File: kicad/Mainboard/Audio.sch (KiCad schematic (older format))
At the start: 66 parts, among them J10 MIC_EXT, J12 SPK_EXT, Q4 BSS138, Q5 BSS138, SW1 INT_PTT_SW, U10 LM386, U8 HEF4066B, U9 OPA340UA

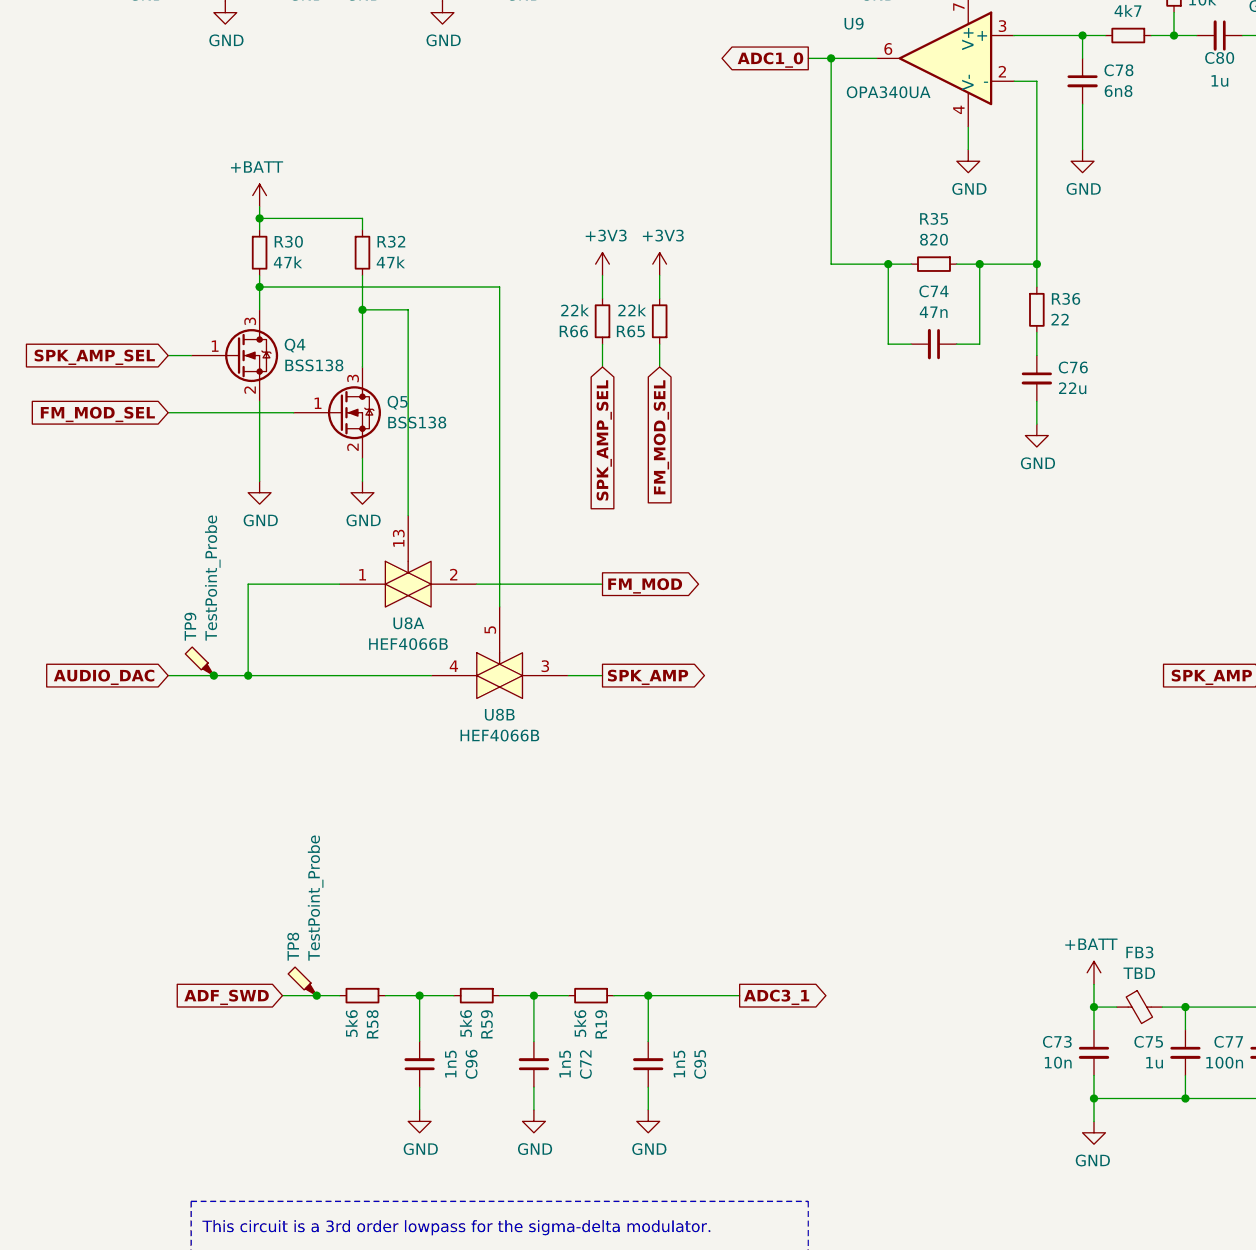
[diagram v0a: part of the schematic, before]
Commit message: added a JCx symbols - these are Jumper Cables - them are used to avoid EMI diseaster when trying to route Power signals under RF 50 ohm trace - also added them to PCB +  Schematic in PDF plotted; TODO - more signal integrity improvement
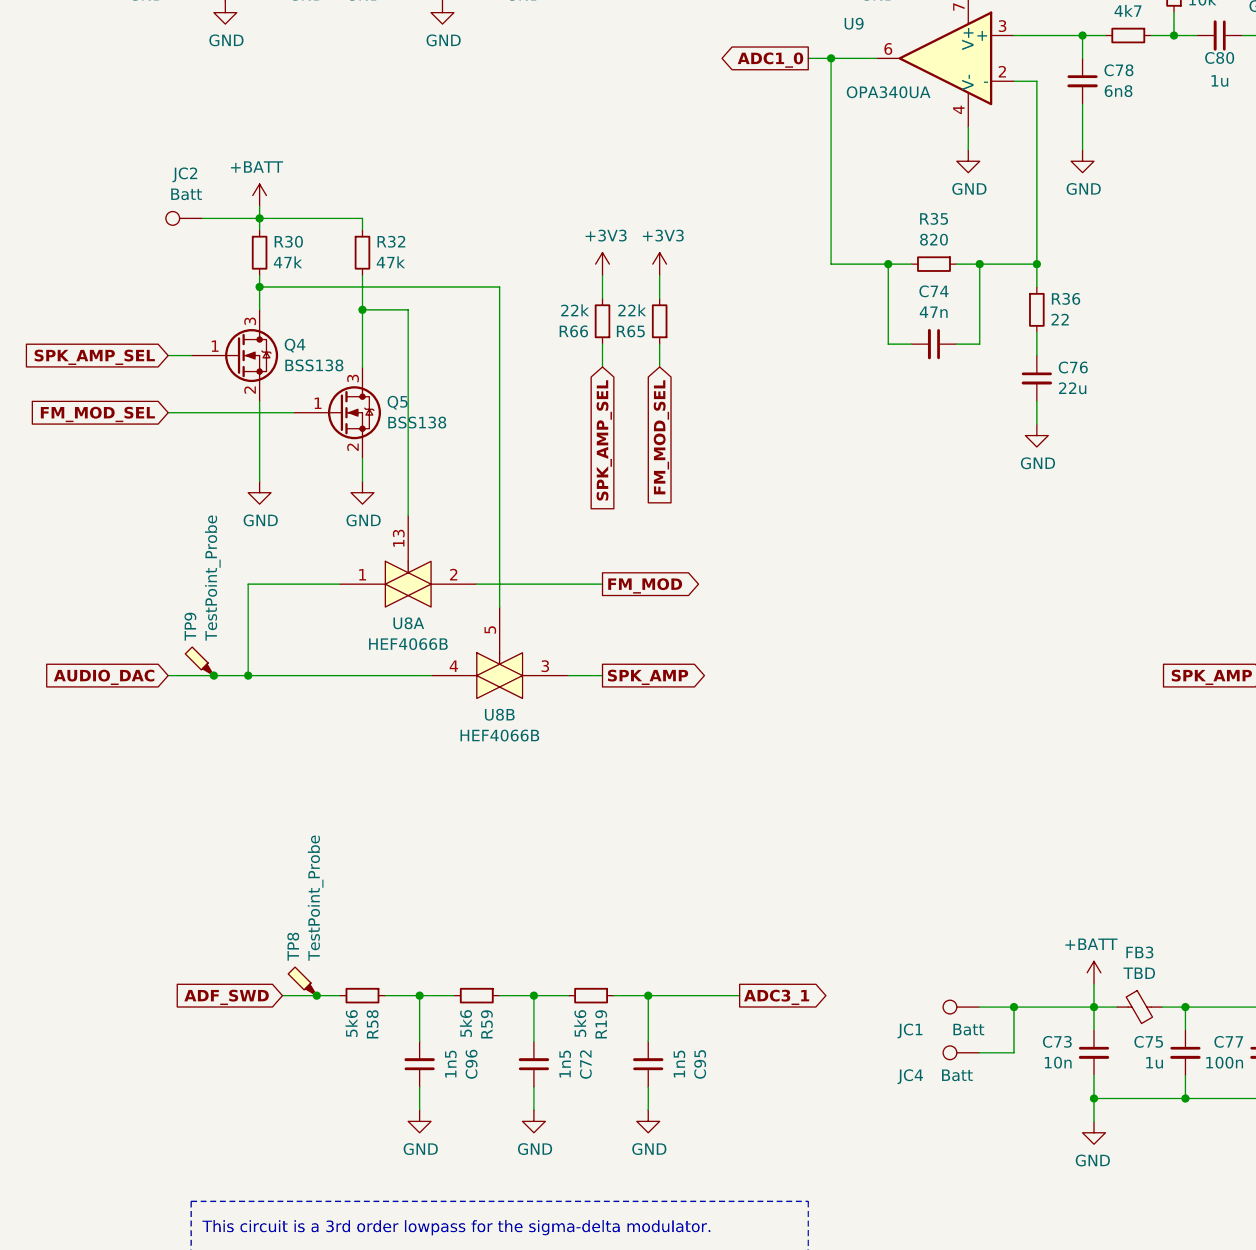
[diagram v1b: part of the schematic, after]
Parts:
- added JC1, JC2, JC4: Batt, TR-9:Pad1x3, symbol Connector:TestPoint
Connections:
- net +BATT: now also JC1.1, JC2.1, JC4.1
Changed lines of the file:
@@
 	3250 6100 3250 6300
 Connection ~ 3250 6100
+$Comp
+L Connector:TestPoint JC2
+U 1 1 5EFA4AA6
+P 1300 2700
+F 0 "JC2" V 1495 2772 50  0000 C CNN
+F 1 "Batt" V 1404 2772 50  0000 C CNN
+F 2 "TR-9:Pad1x3" H 1500 2700 50  0001 C CNN
+F 3 "~" H 1500 2700 50  0001 C CNN
+	1    1300 2700
+	0    -1   -1   0
+$EndComp
+Wire Wire Line
+	1550 2700 1300 2700
+$Comp
+L Connector:TestPoint JC1
+U 1 1 5EFB5A08
+P 4700 6150
+F 0 "JC1" V 4600 6450 50  0000 C CNN
+F 1 "Batt" V 4600 6200 50  0000 C CNN
+F 2 "TR-9:Pad1x3" H 4900 6150 50  0001 C CNN
+F 3 "~" H 4900 6150 50  0001 C CNN
+	1    4700 6150
+	0    -1   -1   0
+$EndComp
+$Comp
+L Connector:TestPoint JC4
+U 1 1 5F06EDAE
+P 4700 6350
+F 0 "JC4" V 4600 6650 50  0000 C CNN
+F 1 "Batt" V 4600 6450 50  0000 C CNN
+F 2 "TR-9:Pad1x3" H 4900 6350 50  0001 C CNN
+F 3 "~" H 4900 6350 50  0001 C CNN
+	1    4700 6350
+	0    -1   -1   0
+$EndComp
+Wire Wire Line
+	4700 6150 4850 6150
+Wire Wire Line
+	4700 6350 4850 6350
+Wire Wire Line
+	4850 6350 4850 6150
+Connection ~ 4850 6150
+Wire Wire Line
+	4850 6150 5200 6150
 $EndSCHEMATC

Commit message: Mainboard: plotted PDF -> added design of PCB -> plotted Gerbers -> Mainboard ready!
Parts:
- added C100: 100n, Capacitor_SMD:C_0603_1608Metric, symbol Mainboard-rescue:C_Small-device
- added C99: 1u, Capacitor_SMD:C_0603_1608Metric, symbol Mainboard-rescue:C_Small-device
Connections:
- net +3V3: now also C100.1, C99.1
- net GND: now also C100.2, C99.2
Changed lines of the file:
@@
 Wire Wire Line
 	4850 6150 5200 6150
+$Comp
+L Mainboard-rescue:C_Small-device C99
+U 1 1 5F4136AC
+P 6950 1300
+F 0 "C99" H 7042 1346 50  0000 L CNN
+F 1 "1u" H 7042 1255 50  0000 L CNN
+F 2 "Capacitor_SMD:C_0603_1608Metric" H 6950 1300 50  0001 C CNN
+F 3 "~" H 6950 1300 50  0001 C CNN
+	1    6950 1300
+	-1   0    0    -1
+$EndComp
+$Comp
+L Mainboard-rescue:C_Small-device C100
+U 1 1 5F4136B2
+P 7300 1300
+F 0 "C100" H 7392 1346 50  0000 L CNN
+F 1 "100n" H 7392 1255 50  0000 L CNN
+F 2 "Capacitor_SMD:C_0603_1608Metric" H 7300 1300 50  0001 C CNN
+F 3 "~" H 7300 1300 50  0001 C CNN
+	1    7300 1300
+	-1   0    0    -1
+$EndComp
+Wire Wire Line
+	7300 1400 7300 1500
+Wire Wire Line
+	6950 1500 6950 1400
+Wire Wire Line
+	7300 1500 7150 1500
+Wire Wire Line
+	6950 1200 7150 1200
+Wire Wire Line
+	7650 1100 7150 1100
+Wire Wire Line
+	7150 1100 7150 1200
+Connection ~ 7150 1200
+Wire Wire Line
+	7150 1200 7300 1200
+$Comp
+L power:GND #PWR0173
+U 1 1 5F444F07
+P 7150 1650
+F 0 "#PWR0173" H 7150 1400 50  0001 C CNN
+F 1 "GND" H 7155 1477 50  0000 C CNN
+F 2 "" H 7150 1650 50  0001 C CNN
+F 3 "" H 7150 1650 50  0001 C CNN
+	1    7150 1650
+	1    0    0    -1
+$EndComp
+Wire Wire Line
+	7150 1650 7150 1500
+Connection ~ 7150 1500
+Wire Wire Line
+	7150 1500 6950 1500
 $EndSCHEMATC

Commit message: added few values in BOM
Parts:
- C100, C14, C73, C77, C82, C85, C90, C91: Tolerance (none) -> 10; Voltage (none) -> 25
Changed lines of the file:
@@
 F 2 "Capacitor_SMD:C_0603_1608Metric" H 9850 1600 50  0001 C CNN
 F 3 "~" H 9850 1600 50  0001 C CNN
+F 4 "25" H 9850 1600 50  0001 C CNN "Voltage"
+F 5 "10" H 9850 1600 50  0001 C CNN "Tolerance"
 	1    9850 1600
 	-1   0    0    1
@@
 F 2 "Capacitor_SMD:C_0603_1608Metric" H 6750 3950 50  0001 C CNN
 F 3 "~" H 6750 3950 50  0001 C CNN
+F 4 "10" H 6750 3950 50  0001 C CNN "Tolerance"
+F 5 "25" H 6750 3950 50  0001 C CNN "Voltage"
 	1    6750 3950
 	-1   0    0    -1
@@
 F 2 "Capacitor_SMD:C_0603_1608Metric" H 7500 3950 50  0001 C CNN
 F 3 "~" H 7500 3950 50  0001 C CNN
+F 4 "25" H 7500 3950 50  0001 C CNN "Voltage"
+F 5 "10" H 7500 3950 50  0001 C CNN "Tolerance"
 	1    7500 3950
 	-1   0    0    -1
@@
 F 2 "Capacitor_SMD:C_0603_1608Metric" H 10200 4050 50  0001 C CNN
 F 3 "~" H 10200 4050 50  0001 C CNN
+F 4 "25" H 10200 4050 50  0001 C CNN "Voltage"
+F 5 "10" H 10200 4050 50  0001 C CNN "Tolerance"
 	1    10200 4050
 	-1   0    0    1
@@
 F 2 "Capacitor_SMD:C_0603_1608Metric" H 5200 6350 50  0001 C CNN
 F 3 "~" H 5200 6350 50  0001 C CNN
+F 4 "10" H 5200 6350 50  0001 C CNN "Tolerance"
+F 5 "25" H 5200 6350 50  0001 C CNN "Voltage"
 	1    5200 6350
 	-1   0    0    -1
@@
 F 2 "Capacitor_SMD:C_0603_1608Metric" H 5950 6350 50  0001 C CNN
 F 3 "~" H 5950 6350 50  0001 C CNN
+F 4 "25" H 5950 6350 50  0001 C CNN "Voltage"
+F 5 "10" H 5950 6350 50  0001 C CNN "Tolerance"
 	1    5950 6350
 	-1   0    0    -1
@@
 F 2 "Capacitor_SMD:C_0603_1608Metric" H 4450 1500 50  0001 C CNN
 F 3 "~" H 4450 1500 50  0001 C CNN
+F 4 "25" H 4450 1500 50  0001 C CNN "Voltage"
+F 5 "10" H 4450 1500 50  0001 C CNN "Tolerance"
 	1    4450 1500
 	0    1    1    0
@@
 F 2 "Capacitor_SMD:C_0603_1608Metric" H 7300 1300 50  0001 C CNN
 F 3 "~" H 7300 1300 50  0001 C CNN
+F 4 "25" H 7300 1300 50  0001 C CNN "Voltage"
+F 5 "10" H 7300 1300 50  0001 C CNN "Tolerance"
 	1    7300 1300
 	-1   0    0    -1

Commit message: Mainboard: List of components -> Added TempCoef types, voltage values and tolerance for capaciors; added power values and tolerance for resistors
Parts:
- C100, C14, C73, C77, C82, C85, C90, C91: TempCoef (none) -> X7R; Voltage 25 -> 50
- C72, C74, C76, C78, C79, C83, C87, C88, C95, C96: TempCoef (none) -> X7R; Voltage (none) -> 50
- C75, C80, C81, C84, C99: TempCoef (none) -> X7R; Tolerance (none) -> 10; Voltage (none) -> 50
- C86, C89: TempCoef (none) -> ELEC; Tolerance (none) -> 10; Voltage (none) -> 10
- R19, R30, R32, R35, R36, R37, R38, R39, R40, R41, R42, R43, R44, R45, R47, R48, R49, R50, R57, R58, R59, R65, R66: Power (none) -> 0.125; Tolerance (none) -> 5
- R46: Power (none) -> 0.5; Tolerance (none) -> 5

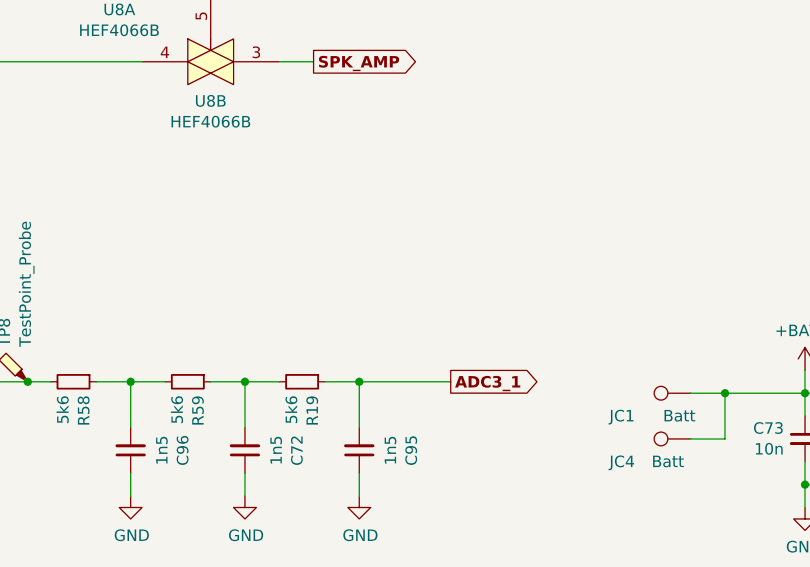
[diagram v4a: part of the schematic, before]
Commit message: Generated Gerbers for new HMI, corrected BOM for Mainboard
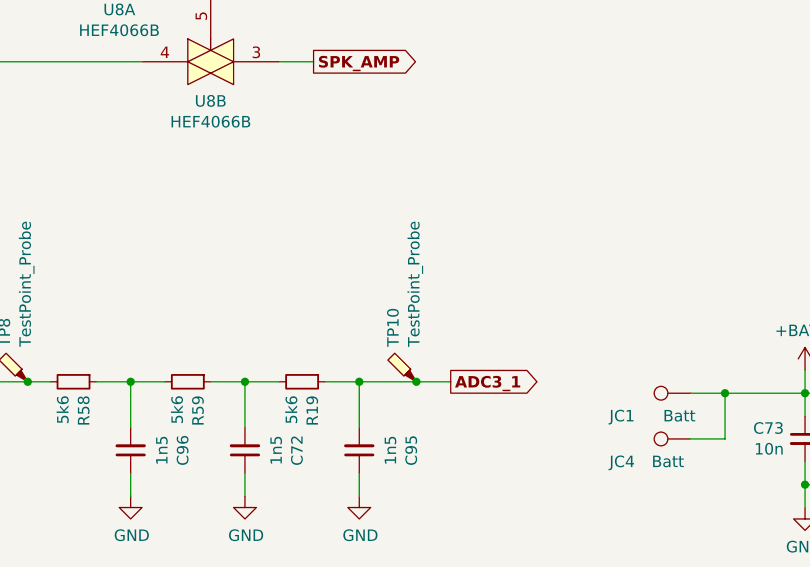
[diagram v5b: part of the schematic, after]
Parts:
- added TP10: TestPoint_Probe, TestPoint:TestPoint_Pad_D1.0mm, symbol Mainboard-rescue:TestPoint_Probe-Connector
- C72, C74, C76, C78, C79, C83, C87, C88, C95, C96: Tolerance (none) -> 10
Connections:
- net ADC3_1: now also TP10.1
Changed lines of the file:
@@
 F 4 "50" H 5150 2100 50  0001 C CNN "Voltage"
 F 5 "X7R" H 5150 2100 50  0001 C CNN "TempCoef"
+F 6 "10" H 5150 2100 50  0001 C CNN "Tolerance"
 	1    5150 2100
 	1    0    0    -1
@@
 F 4 "50" H 5750 1150 50  0001 C CNN "Voltage"
 F 5 "X7R" H 5750 1150 50  0001 C CNN "TempCoef"
+F 6 "10" H 5750 1150 50  0001 C CNN "Tolerance"
 	1    5750 1150
 	0    1    1    0
@@
 F 4 "50" H 4950 3400 50  0001 C CNN "Voltage"
 F 5 "X7R" H 4950 3400 50  0001 C CNN "TempCoef"
+F 6 "10" H 4950 3400 50  0001 C CNN "Tolerance"
 	1    4950 3400
 	1    0    0    -1
@@
 F 4 "50" H 8200 3650 50  0001 C CNN "Voltage"
 F 5 "X7R" H 8200 3650 50  0001 C CNN "TempCoef"
+F 6 "10" H 8200 3650 50  0001 C CNN "Tolerance"
 	1    8200 3650
 	1    0    0    1
@@
 F 4 "50" H 8400 5200 50  0001 C CNN "Voltage"
 F 5 "X7R" H 8400 5200 50  0001 C CNN "TempCoef"
+F 6 "10" H 8400 5200 50  0001 C CNN "Tolerance"
 	1    8400 5200
 	1    0    0    1
@@
 F 4 "50" H 6850 4700 50  0001 C CNN "Voltage"
 F 5 "X7R" H 6850 4700 50  0001 C CNN "TempCoef"
+F 6 "10" H 6850 4700 50  0001 C CNN "Tolerance"
 	1    6850 4700
 	0    -1   -1   0
@@
 F 4 "50" H 3250 6400 50  0001 C CNN "Voltage"
 F 5 "X7R" H 3250 6400 50  0001 C CNN "TempCoef"
+F 6 "10" H 3250 6400 50  0001 C CNN "Tolerance"
 	1    3250 6400
 	-1   0    0    1
@@
 F 4 "50" H 2250 6400 50  0001 C CNN "Voltage"
 F 5 "X7R" H 2250 6400 50  0001 C CNN "TempCoef"
+F 6 "10" H 2250 6400 50  0001 C CNN "Tolerance"
 	1    2250 6400
 	-1   0    0    1
@@
 	3950 7000 3950 7250
 Wire Wire Line
-	3250 6100 3650 6100
+	3250 6100 3500 6100
 $Comp
 L Mainboard-rescue:C_Small-Device C72
@@
 F 4 "50" H 2750 6400 50  0001 C CNN "Voltage"
 F 5 "X7R" H 2750 6400 50  0001 C CNN "TempCoef"
+F 6 "10" H 2750 6400 50  0001 C CNN "Tolerance"
 	1    2750 6400
 	-1   0    0    1
@@
 F 4 "50" H 4500 3250 50  0001 C CNN "Voltage"
 F 5 "X7R" H 4500 3250 50  0001 C CNN "TempCoef"
+F 6 "10" H 4500 3250 50  0001 C CNN "Tolerance"
 	1    4500 3250
 	0    1    1    0
 $EndComp
+$Comp
+L Mainboard-rescue:TestPoint_Probe-Connector TP?
+U 1 1 5F2AA401
+P 3500 6100
+AR Path="/5DF0E505/5F2AA401" Ref="TP?"  Part="1"
+AR Path="/5DFC2ACA/5F2AA401" Ref="TP10"  Part="1"
+F 0 "TP10" H 3653 6201 50  0000 L CNN
+F 1 "TestPoint_Probe" H 3653 6110 50  0000 L CNN
+F 2 "TestPoint:TestPoint_Pad_D1.0mm" H 3700 6100 50  0001 C CNN
+F 3 "~" H 3700 6100 50  0001 C CNN
+	1    3500 6100
+	0    -1   -1   0
+$EndComp
+Connection ~ 3500 6100
+Wire Wire Line
+	3500 6100 3650 6100
 $EndSCHEMATC

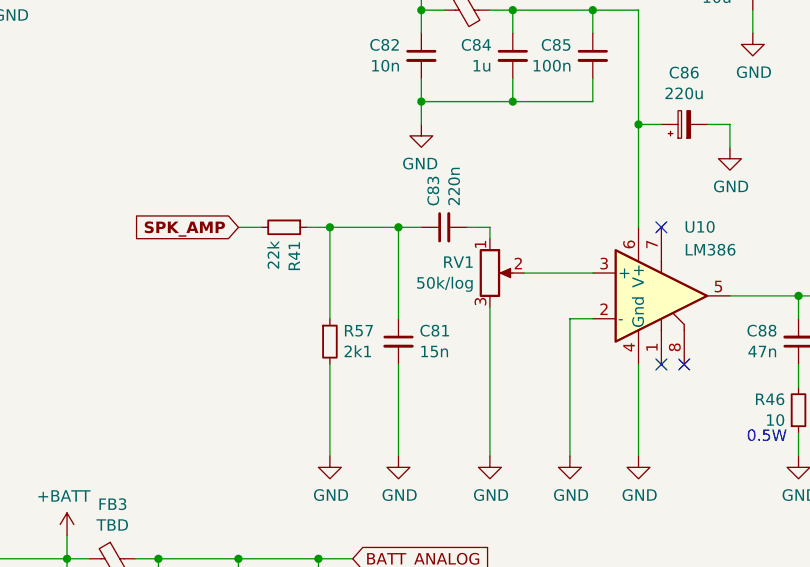
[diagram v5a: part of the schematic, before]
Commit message: Mainboard: corrected C47 & properly described C76, C79, C87 & assigned value to R20 & L1 is now Fair-Rite 2506032217Y2 & Volume pot is now Alps RK0971111Z32
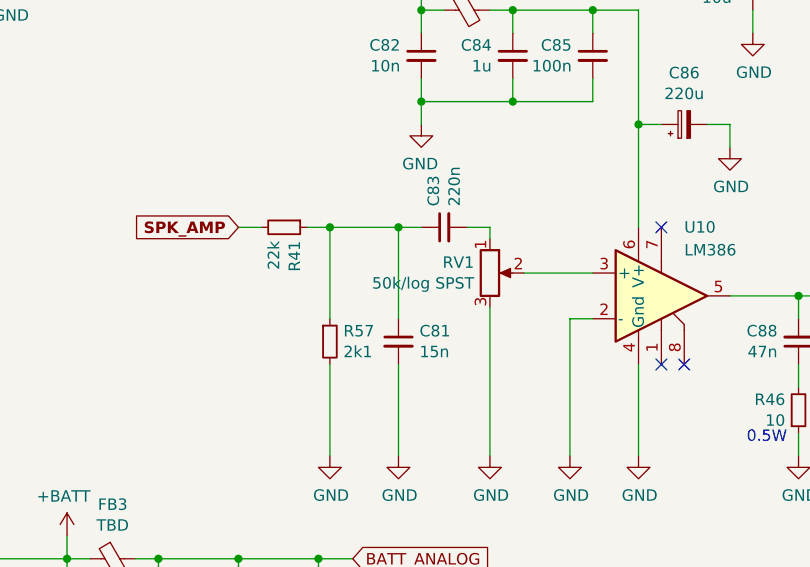
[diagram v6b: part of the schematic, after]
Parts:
- C76, C79, C87: Voltage 50 -> 10
- RV1: value 50k/log -> 50k/log SPST; Partno (none) -> Alps RK0971111Z32
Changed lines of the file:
@@
 F 2 "Capacitor_SMD:C_0603_1608Metric" H 5750 1150 50  0001 C CNN
 F 3 "~" H 5750 1150 50  0001 C CNN
-F 4 "50" H 5750 1150 50  0001 C CNN "Voltage"
+F 4 "10" H 5750 1150 50  0001 C CNN "Voltage"
 F 5 "X7R" H 5750 1150 50  0001 C CNN "TempCoef"
 F 6 "10" H 5750 1150 50  0001 C CNN "Tolerance"
@@
 F 2 "Capacitor_SMD:C_0603_1608Metric" H 4950 3400 50  0001 C CNN
 F 3 "~" H 4950 3400 50  0001 C CNN
-F 4 "50" H 4950 3400 50  0001 C CNN "Voltage"
+F 4 "10" H 4950 3400 50  0001 C CNN "Voltage"
 F 5 "X7R" H 4950 3400 50  0001 C CNN "TempCoef"
 F 6 "10" H 4950 3400 50  0001 C CNN "Tolerance"
@@
 F 2 "Capacitor_SMD:C_0603_1608Metric" H 8200 3650 50  0001 C CNN
 F 3 "~" H 8200 3650 50  0001 C CNN
-F 4 "50" H 8200 3650 50  0001 C CNN "Voltage"
+F 4 "10" H 8200 3650 50  0001 C CNN "Voltage"
 F 5 "X7R" H 8200 3650 50  0001 C CNN "TempCoef"
 F 6 "10" H 8200 3650 50  0001 C CNN "Tolerance"
@@
 P 7050 4900
 F 0 "RV1" H 6981 4946 50  0000 R CNN
-F 1 "50k/log" H 6981 4855 50  0000 R CNN
+F 1 "50k/log SPST" H 6981 4855 50  0000 R CNN
 F 2 "Connector_PinHeader_1.27mm:PinHeader_1x03_P1.27mm_Vertical" H 7050 4900 50  0001 C CNN
 F 3 "~" H 7050 4900 50  0001 C CNN
+F 4 "Alps RK0971111Z32" H 7050 4900 50  0001 C CNN "Partno"
 	1    7050 4900
 	1    0    0    -1

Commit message: Update
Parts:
- removed SW1: INT_PTT_SW, Button_Switch_THT:SW_Tactile_SKHH_Angled, symbol Mainboard-rescue:SW_Push-switches
- added SW1: INT_PTT_SW, Button_Switch_SMD:SW_Push_1P1T_NO_CK_KMR2, symbol Switch:SW_Push
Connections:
- net GND: now also SW1.1
- net at C90.2, R47.1, R48.2: now also SW1.2
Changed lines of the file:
@@
-$EndComp
-$Comp
-L Mainboard-rescue:SW_Push-switches SW1
-U 1 1 5DFE1B21
-P 10500 1650
-F 0 "SW1" V 10450 1400 50  0000 L CNN
-F 1 "INT_PTT_SW" V 10550 1150 50  0000 L CNN
-F 2 "Button_Switch_THT:SW_Tactile_SKHH_Angled" H 10500 1850 50  0001 C CNN
-F 3 "" H 10500 1850 50  0001 C CNN
-	1    10500 1650
-	0    -1   1    0
 $EndComp
 $Comp
@@
 	4550 1500 4650 1500
 Wire Wire Line
-	10500 1850 10500 1900
-Wire Wire Line
 	10500 1450 10500 1400
 Wire Wire Line
@@
 Wire Wire Line
 	3500 6100 3650 6100
+$Comp
+L Switch:SW_Push SW1
+U 1 1 6121661D
+P 10500 1650
+F 0 "SW1" V 10546 1602 50  0000 R CNN
+F 1 "INT_PTT_SW" V 10455 1602 50  0000 R CNN
+F 2 "Button_Switch_SMD:SW_Push_1P1T_NO_CK_KMR2" H 10500 1850 50  0001 C CNN
+F 3 "~" H 10500 1850 50  0001 C CNN
+	1    10500 1650
+	0    -1   -1   0
+$EndComp
+Wire Wire Line
+	10500 1850 10500 1900
 $EndSCHEMATC
